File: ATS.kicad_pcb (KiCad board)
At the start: 2 copper layers, 72.3 x 37.7 mm, 15 parts

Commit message: incorporated libraries
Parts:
- ADAFRUITBUZZER_1: footprint CPT-2212-3TH:adafruit -> AdafruitBuzzer:AdafruitBuzzer
- TEENSY4.1_1: footprint DEV-16771:MODULE_DEV-16771 -> Teensy4.1:Teensy4.1

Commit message: removed graphic
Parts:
- removed the G*** at (114.7, 133.2)

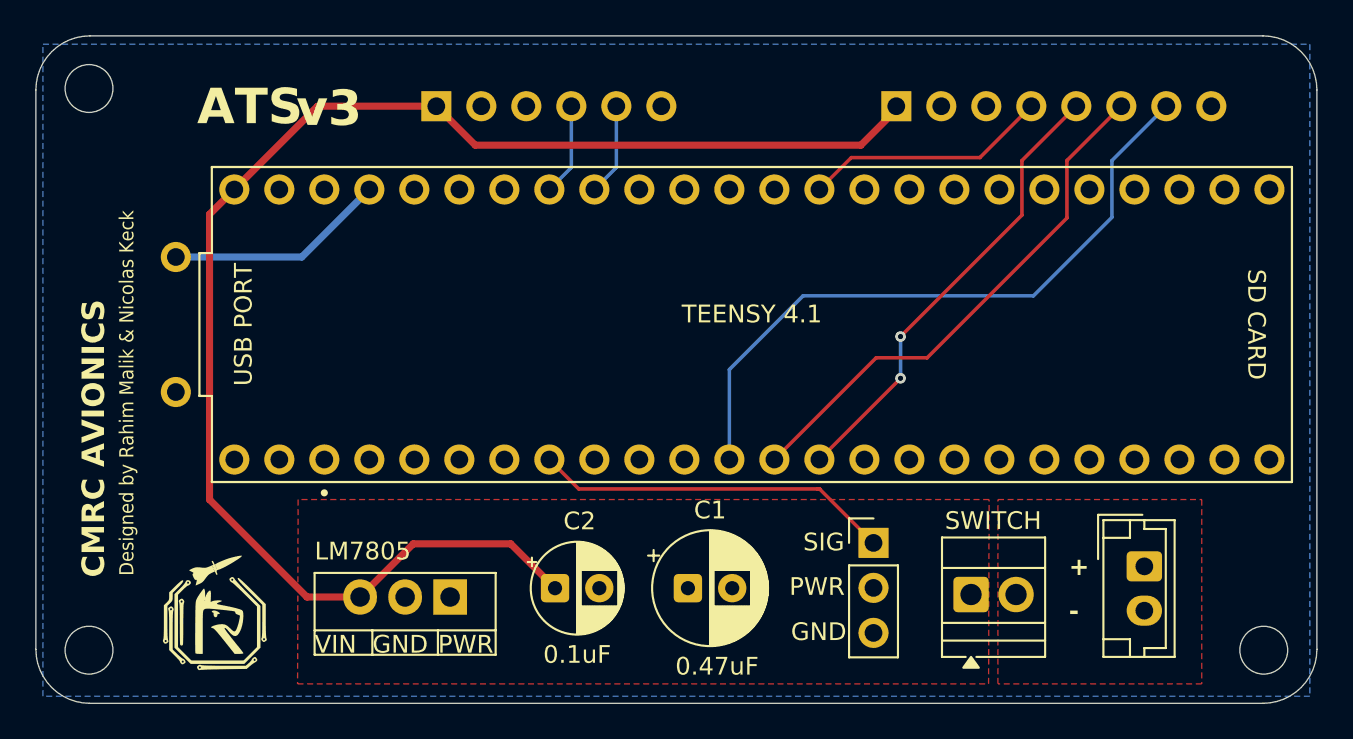
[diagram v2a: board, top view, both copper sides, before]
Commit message: finished review, sent to fab
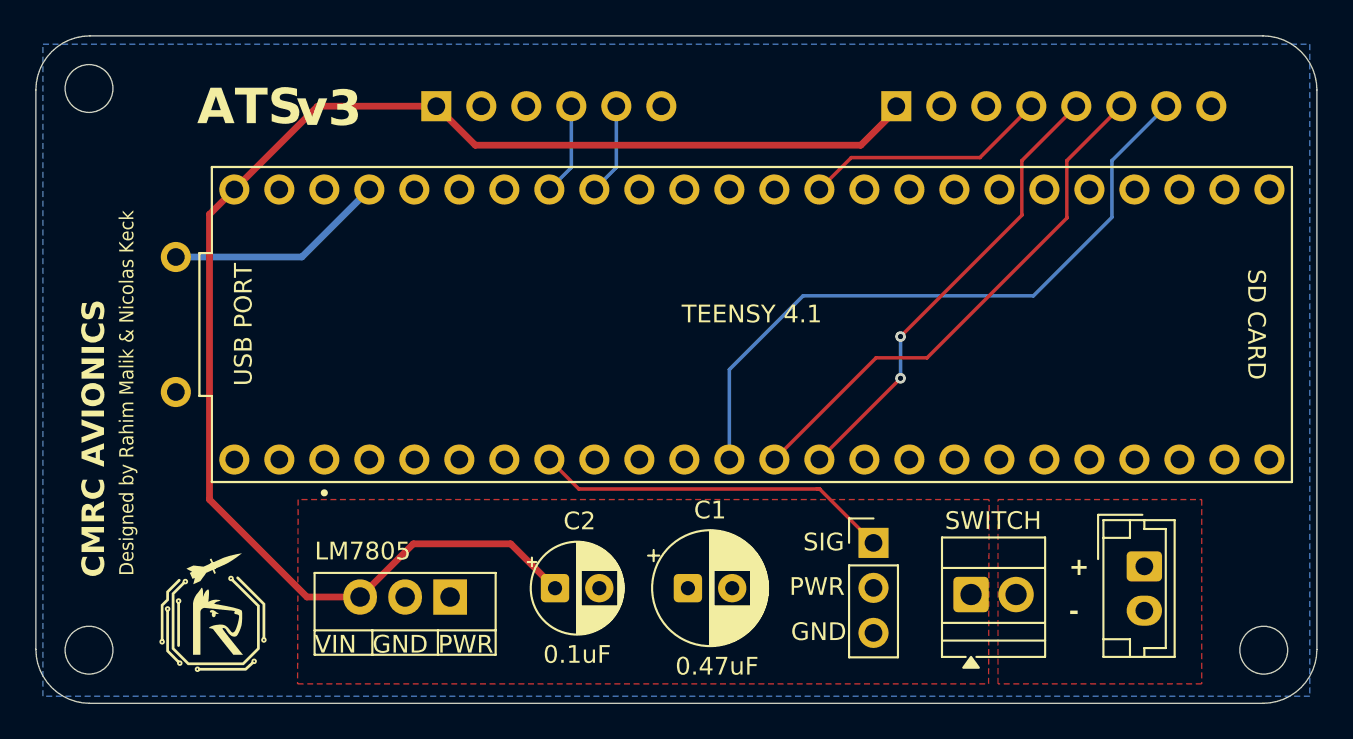
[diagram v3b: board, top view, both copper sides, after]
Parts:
- added svg2mod: G***, Logo:logo, F.Cu at (85.5, 143.4)
- G***: moved to B.Cu
- moved G*** 16.5 mm to (86.6, 130.6), turned to 180 degrees
